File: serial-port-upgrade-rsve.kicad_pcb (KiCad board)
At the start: 4 copper layers, 35.6 x 43.2 mm, 20 parts, among them J1 MFP RC, J2 MFP TDO, J3 VCC, J4 GND, J5 Led, J6 IDC connector, U1 GAL16V8_PHY, U2 12-STAGE_BINARY_RIPPLE_COUNTE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, X1 1,8432 MHz

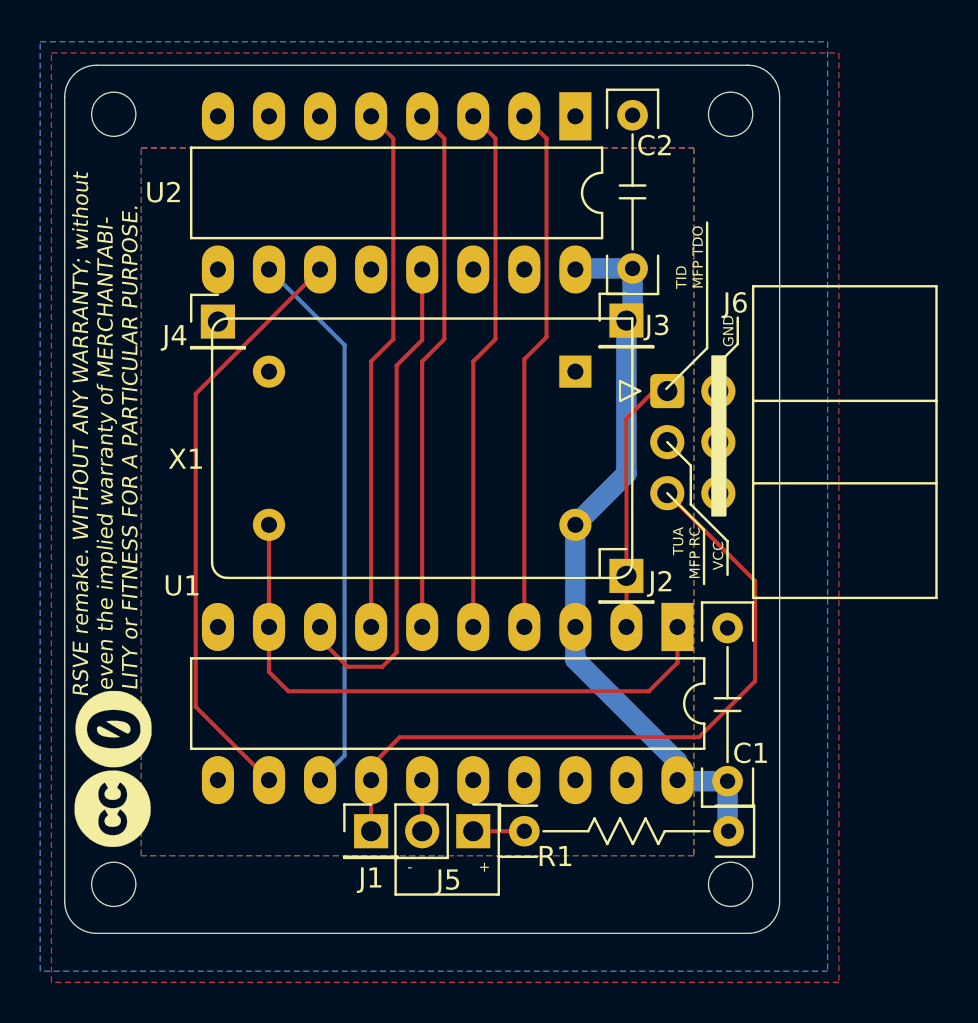
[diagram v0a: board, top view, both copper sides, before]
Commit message: Resolves #1 : Migrate to Kicad 6
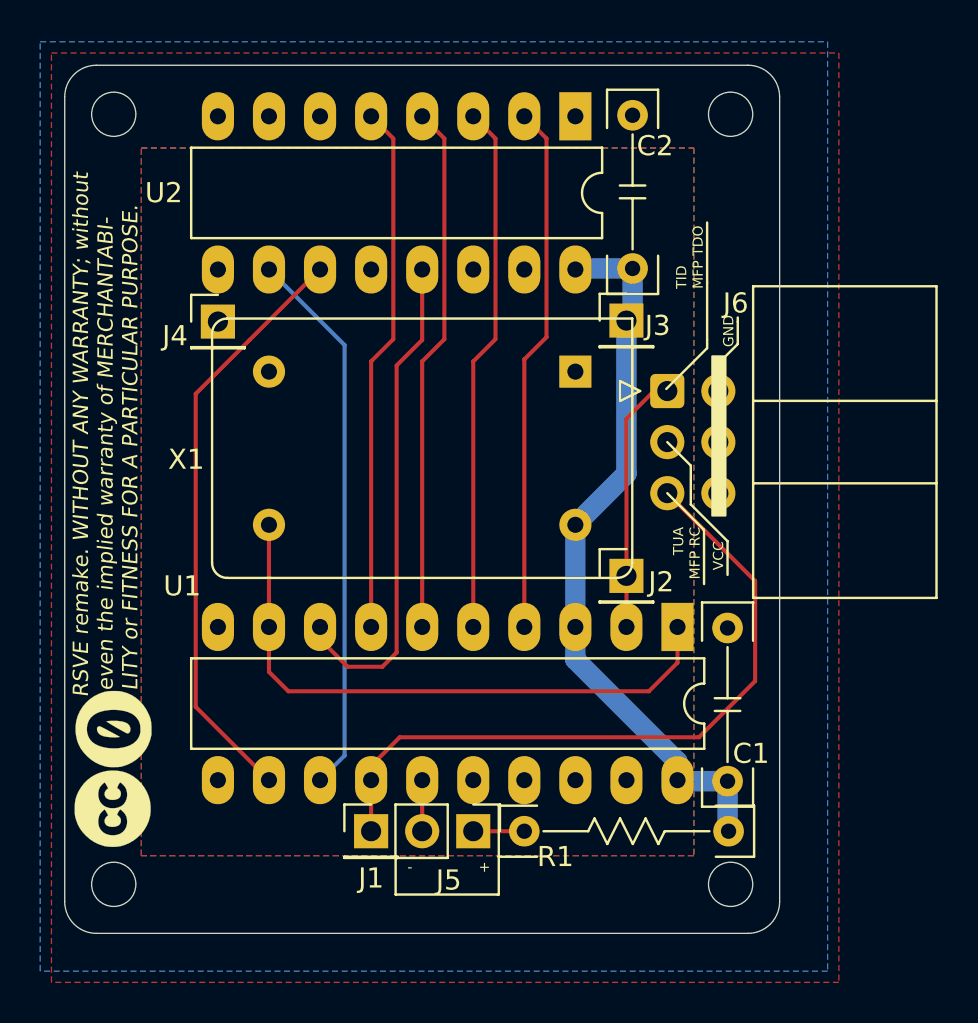
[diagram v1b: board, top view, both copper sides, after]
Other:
- net class Clock removed
- net class Default removed
- net class Power removed
